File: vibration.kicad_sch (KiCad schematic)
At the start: 7 parts, among them J5 Conn_01x02, Q3 SS8050

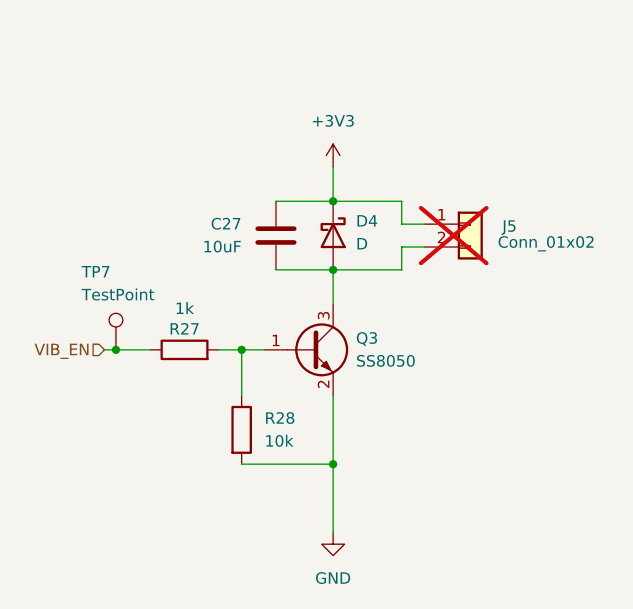
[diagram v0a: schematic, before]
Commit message: extra capacitance vibration, old backlight method
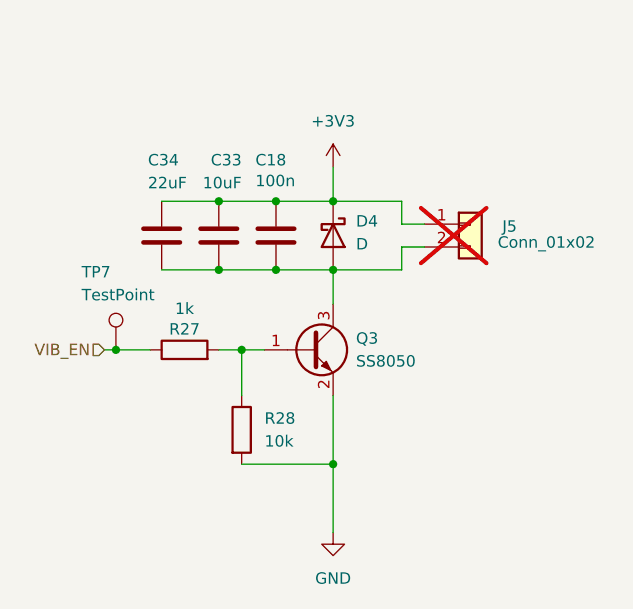
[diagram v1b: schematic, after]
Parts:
- removed C27: 10uF, Capacitor_SMD:C_0603_1608Metric, symbol Device:C
- added C18: 100n, Capacitor_SMD:C_0402_1005Metric, symbol Device:C
- added C33: 10uF, Capacitor_SMD:C_0603_1608Metric, symbol Device:C
- added C34: 22uF, Capacitor_SMD:C_0603_1608Metric, symbol Device:C
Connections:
- net +3V3: now also C18.1, C33.1, C34.1
- net at D4.2 (A), J5.2 (Pin_2), Q3.3 (C): now also C18.2, C33.2, C34.2
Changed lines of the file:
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@@
+	)
+	(junction
+		(at 119.38 71.12)
+		(diameter 0)
+		(color 0 0 0 0)
 	)
 	(junction
@@
 	)
 	(junction
+		(at 125.73 71.12)
+		(diameter 0)
+		(color 0 0 0 0)
+	)
+	(junction
 		(at 121.92 87.63)
+		(diameter 0)
+		(color 0 0 0 0)
+	)
+	(junction
+		(at 125.73 78.74)
 		(diameter 0)
 		(color 0 0 0 0)
@@
 		(color 0 0 0 0)
 	)
+	(junction
+		(at 119.38 78.74)
+		(diameter 0)
+		(color 0 0 0 0)
+	)
 	(wire
 		(pts
@@
 	(wire
 		(pts
+			(xy 119.38 78.74) (xy 125.73 78.74)
+		)
+		(stroke
+			(width 0)
+			(type default)
+		)
+	)
+	(wire
+		(pts
+			(xy 113.03 78.74) (xy 119.38 78.74)
+		)
+		(stroke
+			(width 0)
+			(type default)
+		)
+	)
+	(wire
+		(pts
 			(xy 125.73 78.74) (xy 132.08 78.74)
 		)
@@
 		(pts
 			(xy 107.95 87.63) (xy 111.76 87.63)
+		)
+		(stroke
+			(width 0)
+			(type default)
+		)
+	)
+	(wire
+		(pts
+			(xy 119.38 71.12) (xy 125.73 71.12)
+		)
+		(stroke
+			(width 0)
+			(type default)
+		)
+	)
+	(wire
+		(pts
+			(xy 113.03 71.12) (xy 119.38 71.12)
 		)
 		(stroke
@@
 				(path "/f4643692-c319-40a7-82a2-3e775c0a417f/fa61dece-89ff-456c-a30f-6bfd2f1cc11c"
 					(reference "Q3")
+					(unit 1)
+				)
+			)
+		)
+	)
+	(symbol
+		(lib_id "Device:C")
+		(at 125.73 74.93 0)
+		(unit 1)
+		(exclude_from_sim no)
+		(in_bom yes)
+		(on_board yes)
+		(dnp no)
+		(property "Reference" "C18"
+			(at 123.444 66.548 0)
+			(effects
+				(font
+					(size 1.27 1.27)
+				)
+				(justify left)
+			)
+		)
+		(property "Value" "100n"
+			(at 123.444 68.8594 0)
+			(effects
+				(font
+					(size 1.27 1.27)
+				)
+				(justify left)
+			)
+		)
+		(property "Footprint" "Capacitor_SMD:C_0402_1005Metric"
+			(at 126.6952 78.74 0)
+			(effects
+				(font
+					(size 1.27 1.27)
+				)
+				(hide yes)
+			)
+		)
+		(property "Datasheet" "~"
+			(at 125.73 74.93 0)
+			(effects
+				(font
+					(size 1.27 1.27)
+				)
+				(hide yes)
+			)
+		)
+		(property "Description" ""
+			(at 125.73 74.93 0)
+			(effects
+				(font
+					(size 1.27 1.27)
+				)
+			)
+		)
+		(pin "1"
+		)
+		(pin "2"
+		)
+		(instances
+			(project "gameboy"
+				(path "/f4643692-c319-40a7-82a2-3e775c0a417f/fa61dece-89ff-456c-a30f-6bfd2f1cc11c"
+					(reference "C18")
 					(unit 1)
 				)
@@
 	)
 	(symbol
-		(lib_id "Device:C")
-		(at 125.73 74.93 0)
-		(mirror y)
-		(unit 1)
-		(exclude_from_sim no)
-		(in_bom yes)
-		(on_board yes)
-		(dnp no)
-		(property "Reference" "C27"
-			(at 121.92 73.6599 0)
-			(effects
-				(font
-					(size 1.27 1.27)
-				)
-				(justify left)
-			)
-		)
-		(property "Value" "10uF"
-			(at 121.92 76.1999 0)
-			(effects
-				(font
-					(size 1.27 1.27)
-				)
-				(justify left)
-			)
-		)
-		(property "Footprint" "Capacitor_SMD:C_0603_1608Metric"
-			(at 124.7648 78.74 0)
-			(effects
-				(font
-					(size 1.27 1.27)
-				)
-				(hide yes)
-			)
-		)
-		(property "Datasheet" "~"
-			(at 125.73 74.93 0)
-			(effects
-				(font
-					(size 1.27 1.27)
-				)
-				(hide yes)
-			)
-		)
-		(property "Description" "Unpolarized capacitor"
-			(at 125.73 74.93 0)
-			(effects
-				(font
-					(size 1.27 1.27)
-				)
-				(hide yes)
-			)
-		)
-		(property "LCSC" ""
-			(at 125.73 74.93 0)
-			(effects
-				(font
-					(size 1.27 1.27)
-				)
-				(hide yes)
-			)
-		)
-		(property "Manufacturer" ""
-			(at 125.73 74.93 0)
-			(effects
-				(font
-					(size 1.27 1.27)
-				)
-				(hide yes)
-			)
-		)
-		(property "Manufacturer Part Number" ""
-			(at 125.73 74.93 0)
-			(effects
-				(font
-					(size 1.27 1.27)
-				)
-				(hide yes)
-			)
-		)
-		(pin "2"
-		)
-		(pin "1"
-		)
-		(instances
-			(project "gameboy"
-				(path "/f4643692-c319-40a7-82a2-3e775c0a417f/fa61dece-89ff-456c-a30f-6bfd2f1cc11c"
-					(reference "C27")
-					(unit 1)
-				)
-			)
-		)
-	)
-	(symbol
 		(lib_id "Connector:TestPoint")
 		(at 107.95 87.63 0)
@@
 	)
 	(symbol
+		(lib_id "Device:C")
+		(at 113.03 74.93 0)
+		(unit 1)
+		(exclude_from_sim no)
+		(in_bom yes)
+		(on_board yes)
+		(dnp no)
+		(property "Reference" "C34"
+			(at 111.506 66.548 0)
+			(effects
+				(font
+					(size 1.27 1.27)
+				)
+				(justify left)
+			)
+		)
+		(property "Value" "22uF"
+			(at 111.506 69.088 0)
+			(effects
+				(font
+					(size 1.27 1.27)
+				)
+				(justify left)
+			)
+		)
+		(property "Footprint" "Capacitor_SMD:C_0603_1608Metric"
+			(at 113.9952 78.74 0)
+			(effects
+				(font
+					(size 1.27 1.27)
+				)
+				(hide yes)
+			)
+		)
+		(property "Datasheet" "~"
+			(at 113.03 74.93 0)
+			(effects
+				(font
+					(size 1.27 1.27)
+				)
+				(hide yes)
+			)
+		)
+		(property "Description" "Unpolarized capacitor"
+			(at 113.03 74.93 0)
+			(effects
+				(font
+					(size 1.27 1.27)
+				)
+				(hide yes)
+			)
+		)
+		(property "LCSC" ""
+			(at 113.03 74.93 0)
+			(effects
+				(font
+					(size 1.27 1.27)
+				)
+				(hide yes)
+			)
+		)
+		(property "Manufacturer" ""
+			(at 113.03 74.93 0)
+			(effects
+				(font
+					(size 1.27 1.27)
+				)
+				(hide yes)
+			)
+		)
+		(property "Manufacturer Part Number" ""
+			(at 113.03 74.93 0)
+			(effects
+				(font
+					(size 1.27 1.27)
+				)
+				(hide yes)
+			)
+		)
+		(pin "2"
+		)
+		(pin "1"
+		)
+		(instances
+			(project "gameboy"
+				(path "/f4643692-c319-40a7-82a2-3e775c0a417f/fa61dece-89ff-456c-a30f-6bfd2f1cc11c"
+					(reference "C34")
+					(unit 1)
+				)
+			)
+		)
+	)
+	(symbol
 		(lib_id "Device:R")
 		(at 121.92 96.52 0)
@@
 					(unit 1)
 				)
+			)
+		)
+	)
+	(symbol
+		(lib_id "Device:C")
+		(at 119.38 74.93 0)
+		(mirror y)
+		(unit 1)
+		(exclude_from_sim no)
+		(in_bom yes)
+		(on_board yes)
+		(dnp no)
+		(property "Reference" "C33"
+			(at 121.92 66.548 0)
+			(effects
+				(font
+					(size 1.27 1.27)
+				)
+				(justify left)
+			)
+		)
+		(property "Value" "10uF"
+			(at 121.92 69.088 0)
+			(effects
+				(font
+					(size 1.27 1.27)
+				)
+				(justify left)
+			)
+		)
+		(property "Footprint" "Capacitor_SMD:C_0603_1608Metric"
+			(at 118.4148 78.74 0)
+			(effects
+				(font
+					(size 1.27 1.27)
+				)
+				(hide yes)
+			)
+		)
+		(property "Datasheet" "~"
+			(at 119.38 74.93 0)
+			(effects
+				(font
+					(size 1.27 1.27)
+				)
+				(hide yes)
+			)
+		)
+		(property "Description" "Unpolarized capacitor"
+			(at 119.38 74.93 0)
+			(effects
+				(font
+					(size 1.27 1.27)
+				)
+				(hide yes)
+			)
+		)
+		(property "LCSC" ""
+			(at 119.38 74.93 0)
+			(effects
+				(font
+					(size 1.27 1.27)
+				)
+				(hide yes)
+			)
+		)
+		(property "Manufacturer" ""
+			(at 119.38 74.93 0)
+			(effects
+				(font
+					(size 1.27 1.27)
+				)
+				(hide yes)
+			)
+		)
+		(property "Manufacturer Part Number" ""
+			(at 119.38 74.93 0)
+			(effects
+				(font
+					(size 1.27 1.27)
+				)
+				(hide yes)
+			)
+		)
+		(pin "2"
+		)
+		(pin "1"
+		)
+		(instances
+			(project "gameboy"
+				(path "/f4643692-c319-40a7-82a2-3e775c0a417f/fa61dece-89ff-456c-a30f-6bfd2f1cc11c"
+					(reference "C33")
+					(unit 1)
+				)

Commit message: some small cleanup thingies
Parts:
- C34: value 22uF -> 1uF; footprint Capacitor_SMD:C_0603_1608Metric -> Capacitor_SMD:C_0402_1005Metric; LCSC (none) -> C52923
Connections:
- net +3V3: now also C34.2; no longer C34.1
- net GND: now also C33.2
- net at C18.2, D4.2 (A), J5.2 (Pin_2)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: now also C34.1; no longer C33.2, C34.2
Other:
- moved on the sheet: C33, J5

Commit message: changes for production
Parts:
- TP7: now left out of the parts list
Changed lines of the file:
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@@
 		(unit 1)
 		(exclude_from_sim no)
-		(in_bom yes)
+		(in_bom no)
 		(on_board yes)
 		(dnp no)

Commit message: fix bom
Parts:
- C18: value 100n -> 100nF
- C34: LCSC C52923 -> (none)
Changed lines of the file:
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@@
 			)
 		)
-		(property "Value" "100n"
+		(property "Value" "100nF"
 			(at 123.444 68.8594 0)
 			(effects
@@
 			)
 		)
-		(property "LCSC" "C52923"
+		(property "LCSC" ""
 			(at 119.38 74.93 0)
 			(effects

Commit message: align some components with inventory
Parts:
- C33: footprint Capacitor_SMD:C_0603_1608Metric -> Capacitor_SMD:C_0805_2012Metric
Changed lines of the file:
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@@
 			)
 		)
-		(property "Footprint" "Capacitor_SMD:C_0603_1608Metric"
+		(property "Footprint" "Capacitor_SMD:C_0805_2012Metric"
 			(at 142.5448 64.77 0)
 			(effects
